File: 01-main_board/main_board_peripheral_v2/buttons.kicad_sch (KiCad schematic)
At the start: 13 parts, among them U3 NL37WZ14USG

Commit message: Push to change computers. New schematic.
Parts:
- removed C6: 10uF, Capacitor_SMD:C_0603_1608Metric, symbol Device:C
- removed R2: 1.4KR, Resistor_SMD:R_0402_1005Metric, symbol Device:R_US
- removed R3: 750R, Resistor_SMD:R_0402_1005Metric, symbol Device:R_US
- removed S1: KSC253J_SP_DELTA_LFG, 22XT_Main_Peripheral:KSC253JSPDELTALFG, symbol 22XT_Main:KSC253J_SP_DELTA_LFG
- removed U3: NL37WZ14USG, 22XT_Main_Peripheral:NL37WZ14USG, symbol 22XT_Main:NL37WZ14USG
- added IC1: NL37WZ17USG, SOP50P312X90-8N, symbol NL37WZ17USG:NL37WZ17USG
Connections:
- net 5V_BOOST: now also IC1.8 (VCC)
- net ESP_BOOT_CONTROL: now also IC1.2 (Y3)
- net ESP_RESET_CONTROL: now also IC1.5 (Y2)
- net GND: now also IC1.4 (GND)
- net button_ESP_BOOT: now also IC1.6 (A3)
- net button_ESP_RESET: now also IC1.3 (A2)
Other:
- note added: "Noninverted Schmitt Trigger"
- note removed: "Inverted Schmitt Trigger"

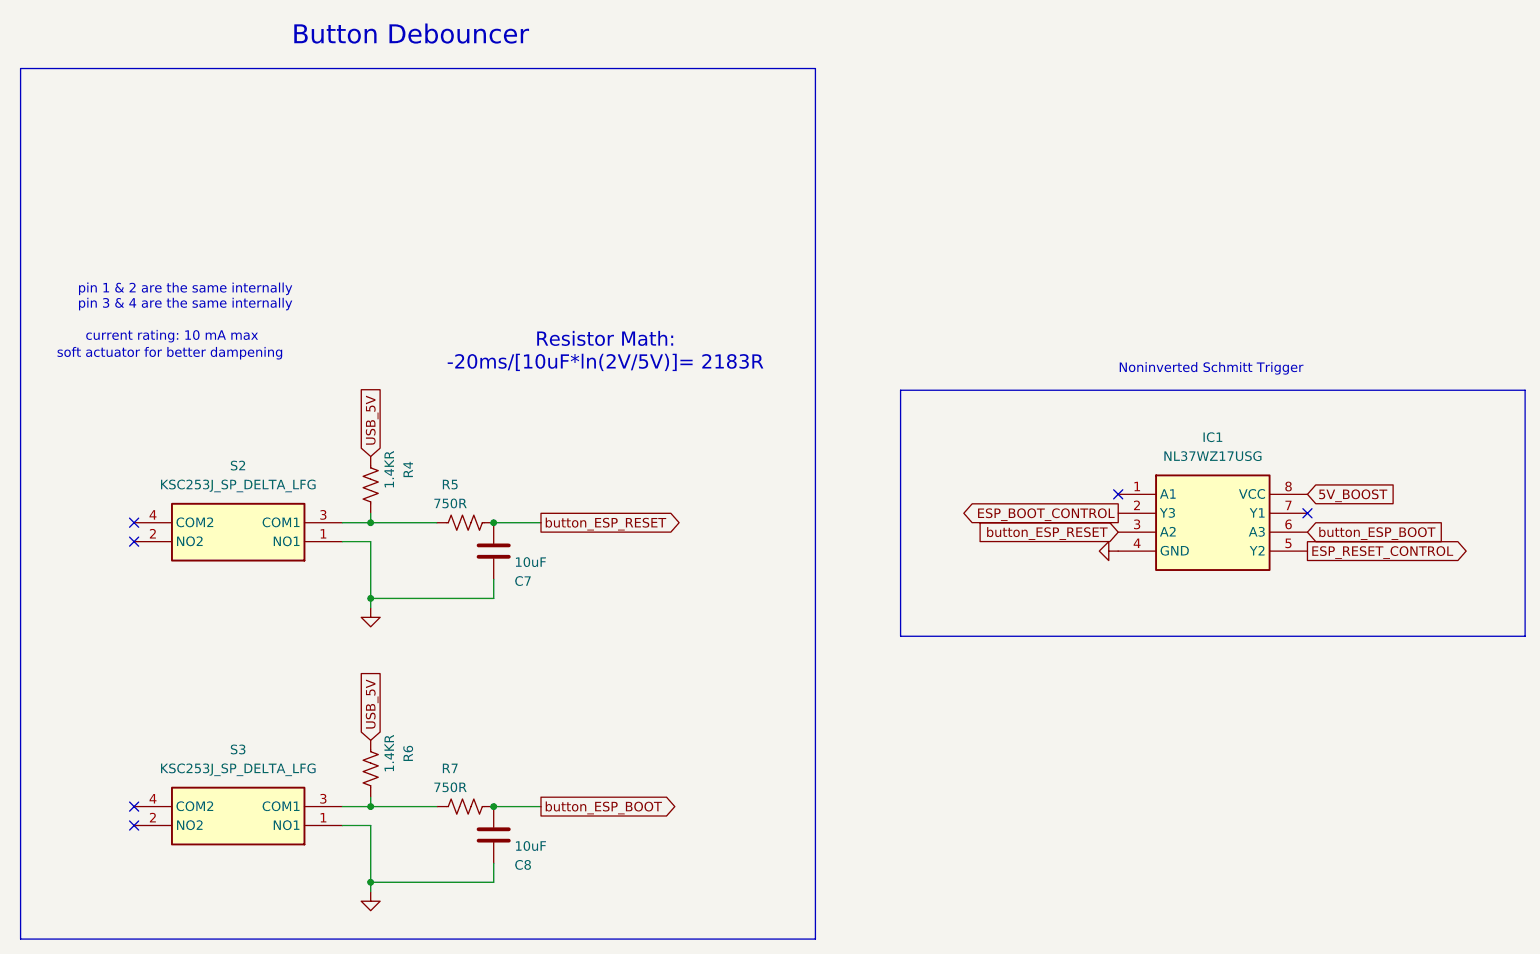
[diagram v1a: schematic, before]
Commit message: Started new layout on version 3
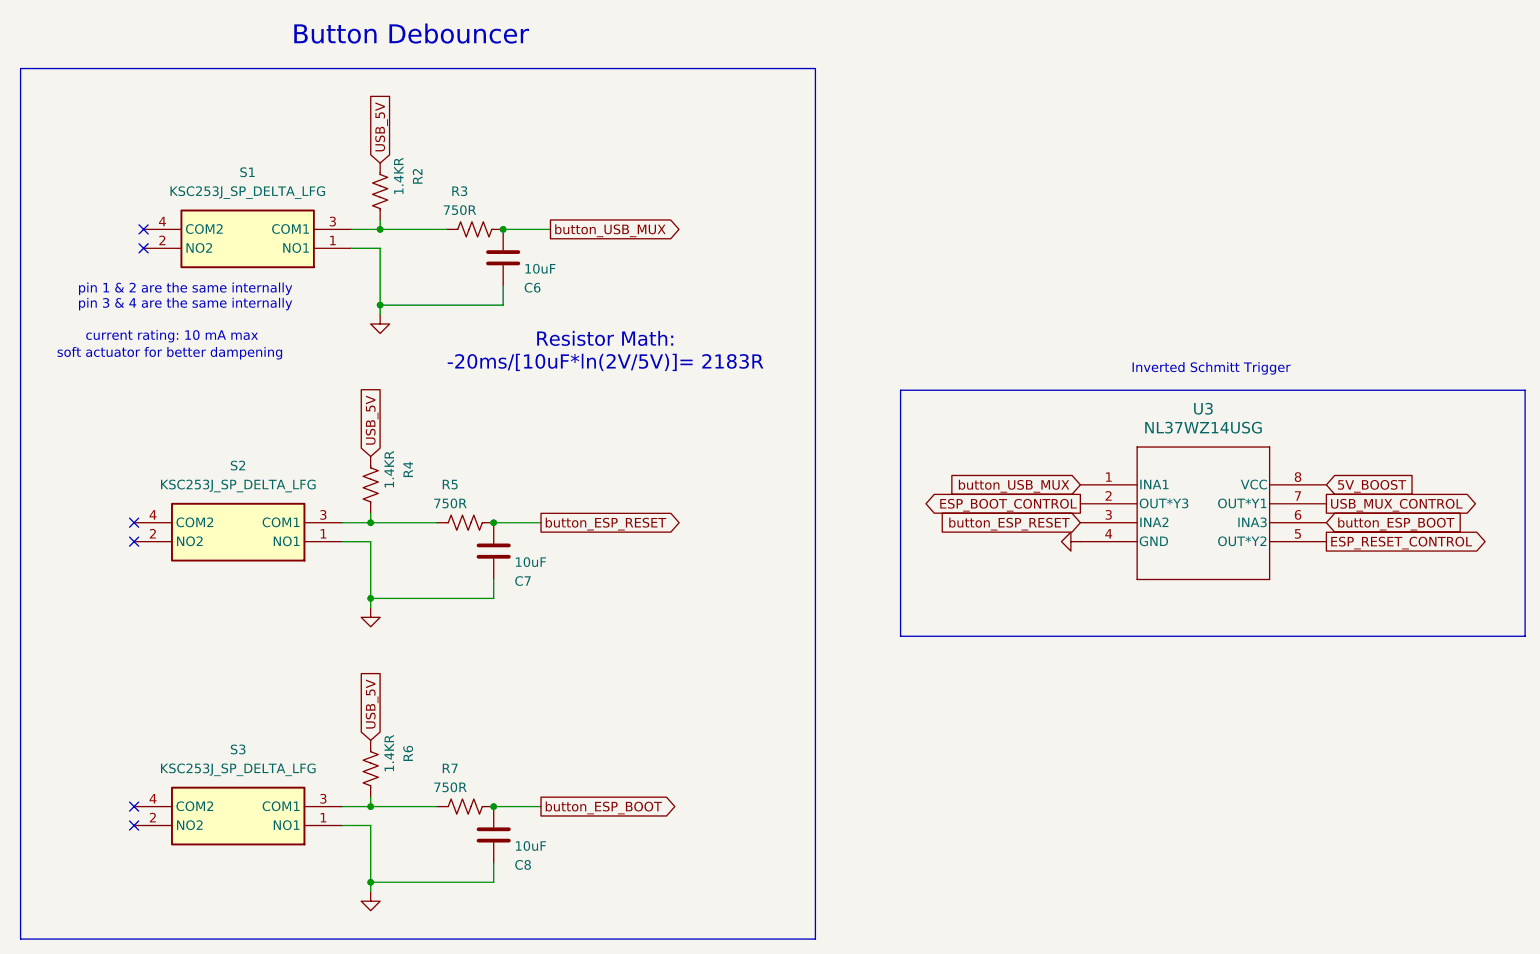
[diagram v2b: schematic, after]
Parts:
- removed IC1: NL37WZ17USG, SOP50P312X90-8N, symbol NL37WZ17USG:NL37WZ17USG
- added C6: 10uF, Capacitor_SMD:C_0603_1608Metric, symbol Device:C
- added R2: 1.4KR, Resistor_SMD:R_0402_1005Metric, symbol Device:R_US
- added R3: 750R, Resistor_SMD:R_0402_1005Metric, symbol Device:R_US
- added S1: KSC253J_SP_DELTA_LFG, 22XT_Main_Peripheral:KSC253JSPDELTALFG, symbol 22XT_Main:KSC253J_SP_DELTA_LFG
- added U3: NL37WZ14USG, 22XT_Main_Peripheral:NL37WZ14USG, symbol 22XT_Main:NL37WZ14USG
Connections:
- net 5V_BOOST: now also U3.8 (VCC)
- net ESP_BOOT_CONTROL: now also U3.2 (OUT*Y3)
- net ESP_RESET_CONTROL: now also U3.5 (OUT*Y2)
- net GND: now also C6.2, S1.1 (NO1), U3.4 (GND)
- net USB_5V: now also R2.1
- net button_ESP_BOOT: now also U3.6 (INA3)
- net button_ESP_RESET: now also U3.3 (INA2)
- new net: R2.2, R3.1, S1.3 (COM1)
- new net USB_MUX_CONTROL: U3.7 (OUT*Y1)
- new net button_USB_MUX: C6.1, R3.2, U3.1 (INA1)
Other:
- note added: "Inverted Schmitt Trigger"
- note removed: "Noninverted Schmitt Trigger"
